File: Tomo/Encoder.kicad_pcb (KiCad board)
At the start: 2 copper layers, 24 x 24 mm, 11 parts, among them J1 CONN_01X04, J201 CONN_01X01, J202 CONN_01X01, U000 QRE1113, U100 QRE1113

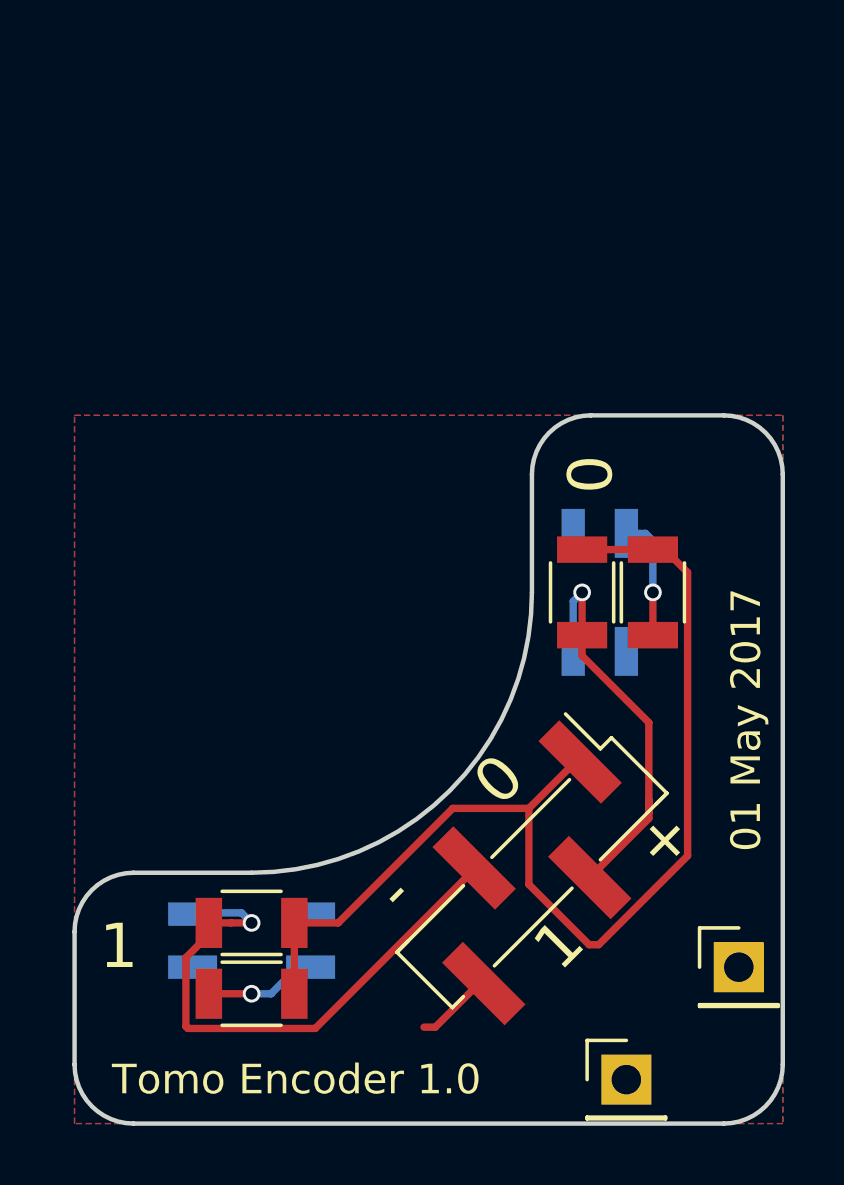
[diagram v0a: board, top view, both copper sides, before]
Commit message: Adding BOM submodule
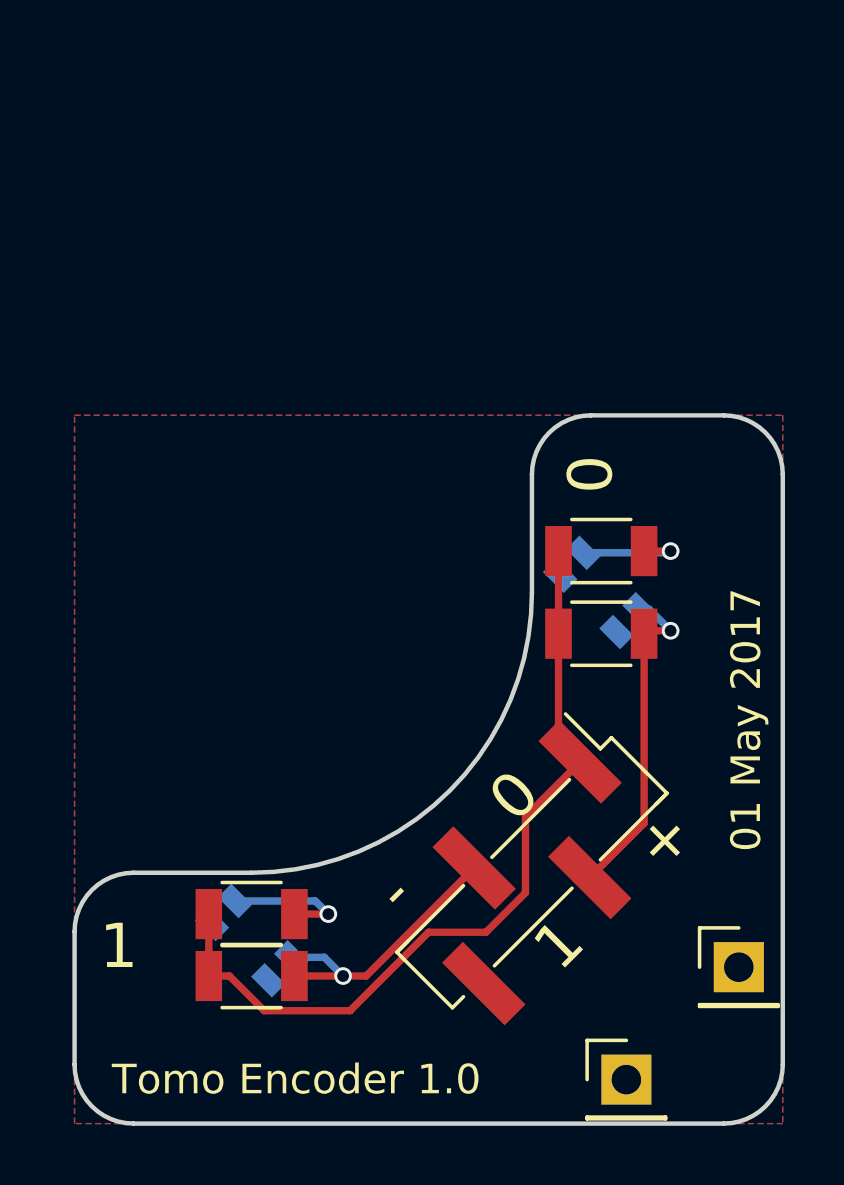
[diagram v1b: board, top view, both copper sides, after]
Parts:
- U000, U100: footprint KwanSystems:QRE1113 -> KwanSystems:EE-SY199
- moved R101 2.70 mm to (100.0, 110.9), turned to 0 degrees
- moved R001 2.24 mm to (111.8, 98.6), turned to 0 degrees
- moved R103 1.80 mm to (100.0, 113.0), turned to 0 degrees
- moved R003 1.54 mm to (111.8, 101.4), turned to 0 degrees
- turned U000 to 135 degrees
- turned U100 to 135 degrees
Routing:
- net VCC: track 38.0 -> 27.6 mm
- net /ENC1: track 20.0 -> 10.2 mm
- net /ENC0: track 14.4 -> 11.6 mm
- net GND: track 2.70 -> 0.00 mm
- net /D0: track 4.90 -> 3.96 mm
- net /D1: track 3.82 -> 4.50 mm

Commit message: Redid encoder to use RP2 parts
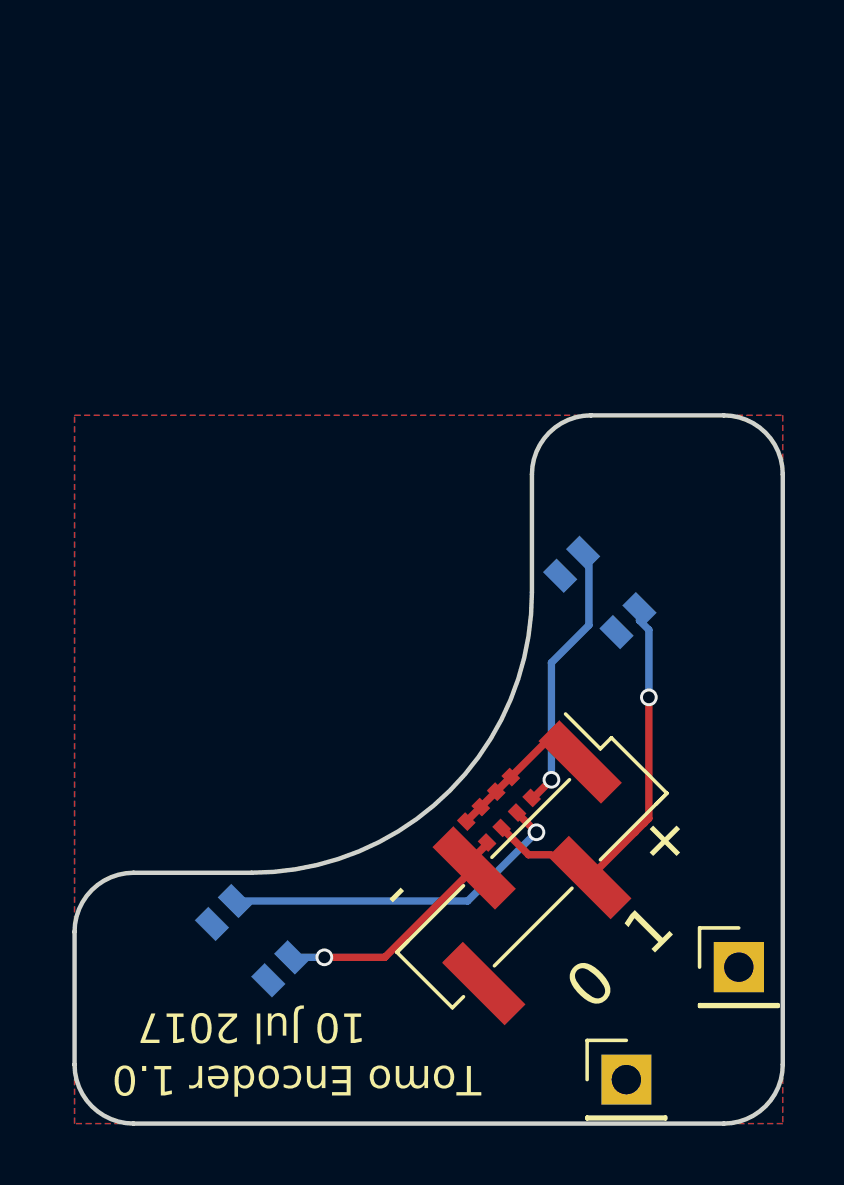
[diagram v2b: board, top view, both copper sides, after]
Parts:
- removed G***: LOGO, KwanSystems:KWAN_CIRCLE_soldermask
- removed R001, R101: 220, Resistors_SMD:R_1206
- removed R003, R103: 10k, Resistors_SMD:R_1206
- removed REF***: OSHW-Symbol_6.7x6mm_SilkScreen, Symbols:OSHW-Symbol_6.7x6mm_SilkScreen
- added R1: 10k, KwanSystems:R_Array_Convex_2x0402, F.Cu at (107.9, 107.9)
- added R2: 220, KwanSystems:R_Array_Convex_2x0402, F.Cu at (108.9, 106.9)
- added U1: KwanSystems, KwanSystems:KWAN_CIRCLE_soldermask, F.Cu at (113.7, 98.2)
- renumbered U100 to U000, U000 to U100
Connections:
- J1 pad 2: /ENC0 -> /ENC1
- J1 pad 3: /ENC1 -> /ENC0
- U000 pad 1: /D1 -> /D0
- U000 pad 3: /ENC1 -> /ENC0
- U100 pad 1: /D0 -> /D1
- U100 pad 3: /ENC0 -> /ENC1
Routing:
- net VCC: track 27.6 -> 4.76 mm
- net /D0: track 3.96 -> 12.1 mm
- net /D1: track 4.50 -> 9.22 mm
- net /ENC0: track 11.6 -> 9.09 mm
- net /ENC1: track 10.2 -> 12.1 mm
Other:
- board text added: "10 Jul 2017"
- board text removed: "01 May 2017"

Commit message: Files as ordered
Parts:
- moved J201 29.5 mm to (116.5, 87.3), turned to 90 degrees
- moved J202 29.5 mm to (112.7, 83.5), turned to 90 degrees
- moved U1 19.7 mm to (98.2, 86.0), turned to 0 degrees
- moved J1 19.0 mm to (109.5, 90.5), turned to 45 degrees
- moved U000 16.7 mm to (111.8, 100.0), turned to 225 degrees
- moved U100 16.7 mm to (100.0, 88.2), turned to 225 degrees
- moved R2 15.9 mm to (106.9, 91.1), turned to 45 degrees
- moved R1 15.7 mm to (107.9, 92.1), turned to 45 degrees
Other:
- outline, holes or cut-outs redrawn

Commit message: Tomo soldermask fix, adding kwire stuff
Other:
- rule pad_to_mask_clearance: 0.2 -> 0
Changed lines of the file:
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@@
-(kicad_pcb (version 20170123) (host pcbnew no-vcs-found-5d25263~58~ubuntu17.04.1)
+(kicad_pcb (version 4) (host pcbnew 4.0.5+dfsg1-4)
   (general
+    (links 16)
+    (no_connects 0)
+    (area 90.629499 78.456666 120.100001 120.100001)
     (thickness 1.6)
     (drawings 22)
@@
     (pad_size 1.7 1.7)
     (pad_drill 1)
-    (pad_to_mask_clearance 0.2)
+    (pad_to_mask_clearance 0)
     (aux_axis_origin 0 0)
     (grid_origin 100 100)
@@
       (hpglpenspeed 20)
       (hpglpendiameter 15)
+      (hpglpenoverlay 2)
       (psnegative false)
       (psa4output false)

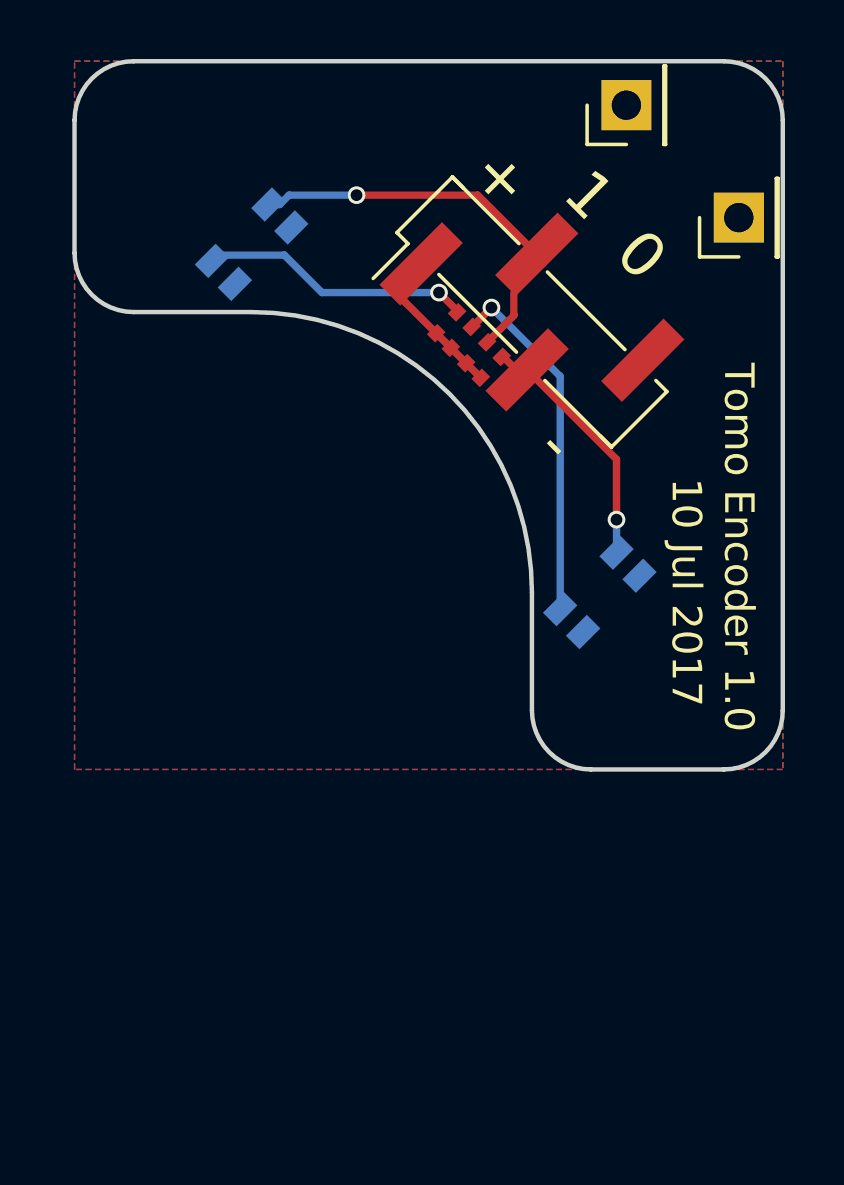
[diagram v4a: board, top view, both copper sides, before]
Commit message: Rework to solve solder mask problem and use 1206 parts
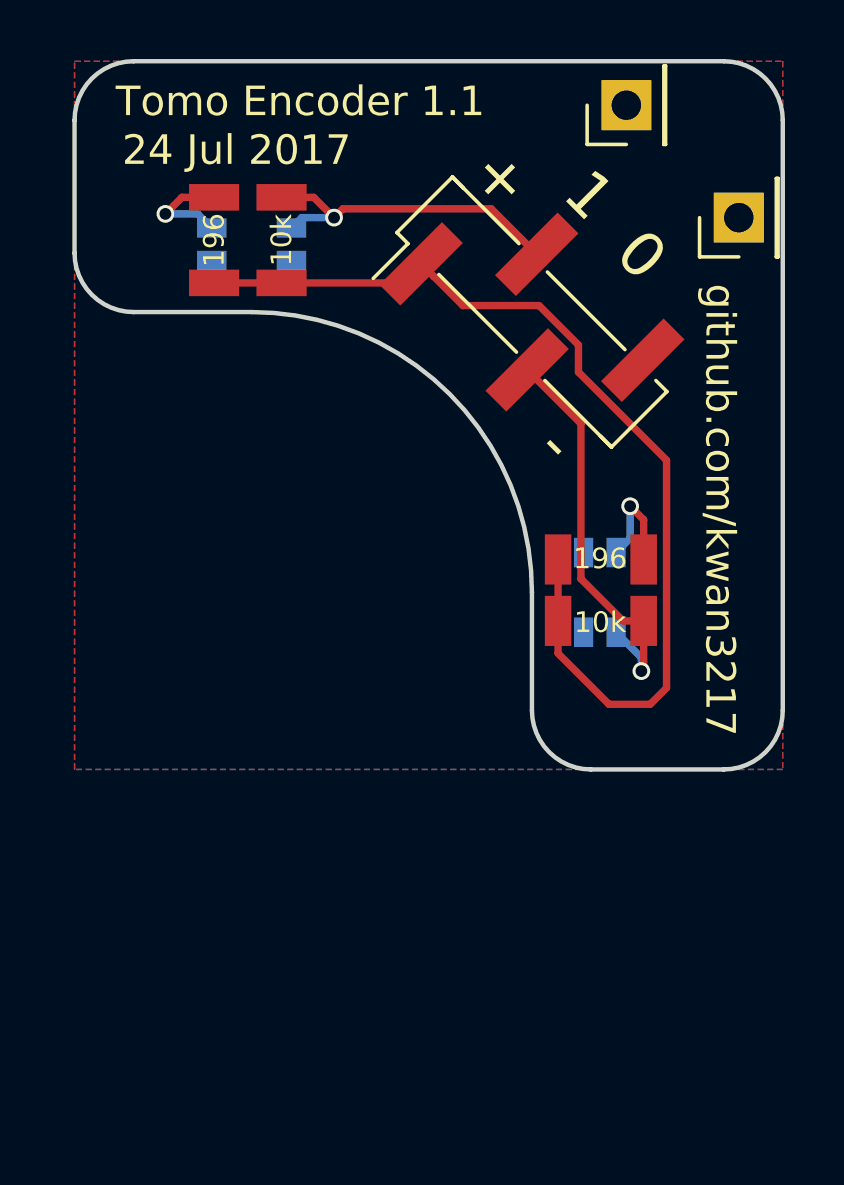
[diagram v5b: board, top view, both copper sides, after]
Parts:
- removed R1: 10k, KwanSystems:R_Array_Convex_2x0402
- removed R2: 220, KwanSystems:R_Array_Convex_2x0402
- removed U1: KwanSystems, KwanSystems:KWAN_CIRCLE_soldermask
- added R001: 196, KwanSystems:SMD_1206, F.Cu at (111.8, 98.9)
- added R003: 10k, KwanSystems:SMD_1206, F.Cu at (111.8, 101.0)
- added R101: 196, KwanSystems:SMD_1206, F.Cu at (98.7, 88.1)
- added R103: 10k, KwanSystems:SMD_1206, F.Cu at (101.0, 88.1)
- U000, U100: value QRE1113 -> EE-SY199
- turned U000 to 90 degrees
- turned U100 to 180 degrees
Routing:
- net VCC: track 4.76 -> 36.0 mm
- net /D0: track 12.1 -> 3.76 mm
- net /ENC0: track 9.09 -> 14.9 mm
- net /D1: track 9.22 -> 3.65 mm
- net /ENC1: track 12.1 -> 11.3 mm
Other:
- rule trace_min: 0.2 -> 0.1524
- board text added: "24 Jul 2017"
- board text added: "Tomo Encoder 1.1"
- board text added: "github.com/kwan3217"
- board text removed: "10 Jul 2017"
- board text removed: "Tomo Encoder 1.0"
